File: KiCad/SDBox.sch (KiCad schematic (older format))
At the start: 18 parts, among them J1 DB25_Male, J2 Micro_SD_Card_Socket, U1 Rapberry_Pi_Pico_2W, U2 SN74CBT16210

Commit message: Add UART0_TX and UART0_RX through level shifter
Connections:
- net GND: no longer U2.7 (1A6), U2.9 (1A7)
- net RESET: now also U2.9 (1A7); no longer U2.6 (1A5)
- net RESET_3V3: now also U2.39 (1B7); no longer U2.42 (1B5)
- net UART0_TX_3V3: now reaches U1.16 (GP12)
- net UART0_TX_3V3: now also U2.42 (1B5)
- net UART0_RX_3V3: now reaches U1.17 (GP13)
- net UART0_RX_3V3: now also U2.40 (1B6)
- new net UART0_RX: U2.7 (1A6)
- new net UART0_TX: U2.6 (1A5)
- no-connect marks 12 -> 16
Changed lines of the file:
@@
 Text GLabel 7450 3600 1    50   Input ~ 0
 MOSI
-Text GLabel 2750 3450 0    50   BiDi ~ 0
-SELECT
 Text GLabel 7250 3600 1    50   Input ~ 0
 SCK
@@
 	1    0    0    -1
 $EndComp
-Text GLabel 3750 3550 2    50   BiDi ~ 0
-SELECT_3V3
 Text GLabel 3750 3350 2    50   BiDi ~ 0
 BUSY_3V3
@@
 Text GLabel 3750 3250 2    50   Input ~ 0
 ACK_3V3
-Text GLabel 2750 3550 0    50   Input ~ 0
+Text GLabel 2750 3850 0    50   Input ~ 0
 RESET
-Text GLabel 3750 3650 2    50   Output ~ 0
+Text GLabel 3750 3950 2    50   Output ~ 0
 RESET_3V3
 $Comp
@@
 $EndComp
 Wire Wire Line
-	2750 3650 2750 3750
-Wire Wire Line
-	2750 3750 2750 3850
-Connection ~ 2750 3750
-Connection ~ 2750 3850
-Wire Wire Line
-	2750 3850 2750 3950
-Connection ~ 2750 3950
-Wire Wire Line
 	2750 3950 2750 4050
 Connection ~ 2750 4050
@@
 NoConn ~ 3750 4150
 NoConn ~ 3750 4050
-NoConn ~ 3750 3950
-NoConn ~ 3750 3850
 $Comp
 L Device:D_Small D3
@@
 Text Label 2400 4450 0    50   ~ 0
 4V3
+NoConn ~ 4800 5200
+NoConn ~ 5800 4600
+NoConn ~ 5800 4400
+NoConn ~ 5800 4200
+NoConn ~ 5800 4100
+NoConn ~ 5800 3800
+Text GLabel 4800 4800 0    50   Output ~ 0
+UART0_TX_3V3
+Text GLabel 4800 4900 0    50   Input ~ 0
+UART0_RX_3V3
+Text GLabel 2750 3950 0    50   Input ~ 0
+GND
+Text GLabel 3750 3650 2    50   Input ~ 0
+UART0_TX_3V3
+Text GLabel 2750 3550 0    50   Output ~ 0
+UART0_TX
+Text GLabel 3750 3550 2    50   BiDi ~ 0
+SELECT_3V3
+Text GLabel 3750 3850 2    50   Output ~ 0
+UART0_RX_3V3
+Text GLabel 2750 3650 0    50   Input ~ 0
+UART0_RX
+Text GLabel 2750 3450 0    50   BiDi ~ 0
+SELECT
 $EndSCHEMATC

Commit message: Add UART pinheader on underside with TX0 (GP12), RX0 (GP13) and Power and GND
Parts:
- added J3: Conn_01x05, SDBox:UART_PinHeader_SMD_pads_2.54mm_pitch, symbol Connector_Generic:Conn_01x05
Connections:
- net +3V3: now also J3.1 (Pin_1)
- net +5V: now also J3.5 (Pin_5)
- net GND: now also J3.3 (Pin_3)
- net UART0_RX: now also J3.4 (Pin_4)
- net UART0_TX: now also J3.2 (Pin_2)
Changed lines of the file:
@@
 Text GLabel 2750 3450 0    50   BiDi ~ 0
 SELECT
+$Comp
+L Connector_Generic:Conn_01x05 J3
+U 1 1 6857FA47
+P 2900 6000
+F 0 "J3" V 2864 5712 50  0000 R CNN
+F 1 "Conn_01x05" V 2773 5712 50  0000 R CNN
+F 2 "SDBox:UART_PinHeader_SMD_pads_2.54mm_pitch" H 2900 6000 50  0001 C CNN
+F 3 "~" H 2900 6000 50  0001 C CNN
+	1    2900 6000
+	0    -1   -1   0
+$EndComp
+Text GLabel 2800 6200 3    50   Output ~ 0
+UART0_TX
+Text GLabel 3100 6200 3    50   Input ~ 0
+VCC
+Text GLabel 2900 6200 3    50   Input ~ 0
+GND
+Text GLabel 2700 6200 3    50   Input ~ 0
+3V3
+Text GLabel 3000 6200 3    50   Input ~ 0
+UART0_RX
 $EndSCHEMATC

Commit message: Improve routing
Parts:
- renumbered D2 to D1, D1 to D2
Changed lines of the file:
@@
 NoConn ~ 1550 3100
 $Comp
-L Device:LED D2
+L Device:LED D1
 U 1 1 5EBAFFCE
 P 8850 3150
-F 0 "D2" V 8889 3033 50  0000 R CNN
+F 0 "D1" V 8889 3033 50  0000 R CNN
 F 1 "Power LED indicator" V 8798 3033 50  0000 R CNN
 F 2 "LED_THT:LED_Rectangular_W5.0mm_H2.0mm" H 8850 3150 50  0001 C CNN
@@
 GND
 $Comp
-L Device:LED D1
+L Device:LED D2
 U 1 1 5EBA7223
 P 9100 4850
-F 0 "D1" V 9100 5000 50  0000 R CNN
+F 0 "D2" V 9100 5000 50  0000 R CNN
 F 1 "Activity LED indicator" V 9350 5150 50  0000 R CNN
 F 2 "LED_THT:LED_Rectangular_W5.0mm_H2.0mm" H 9100 4850 50  0001 C CNN

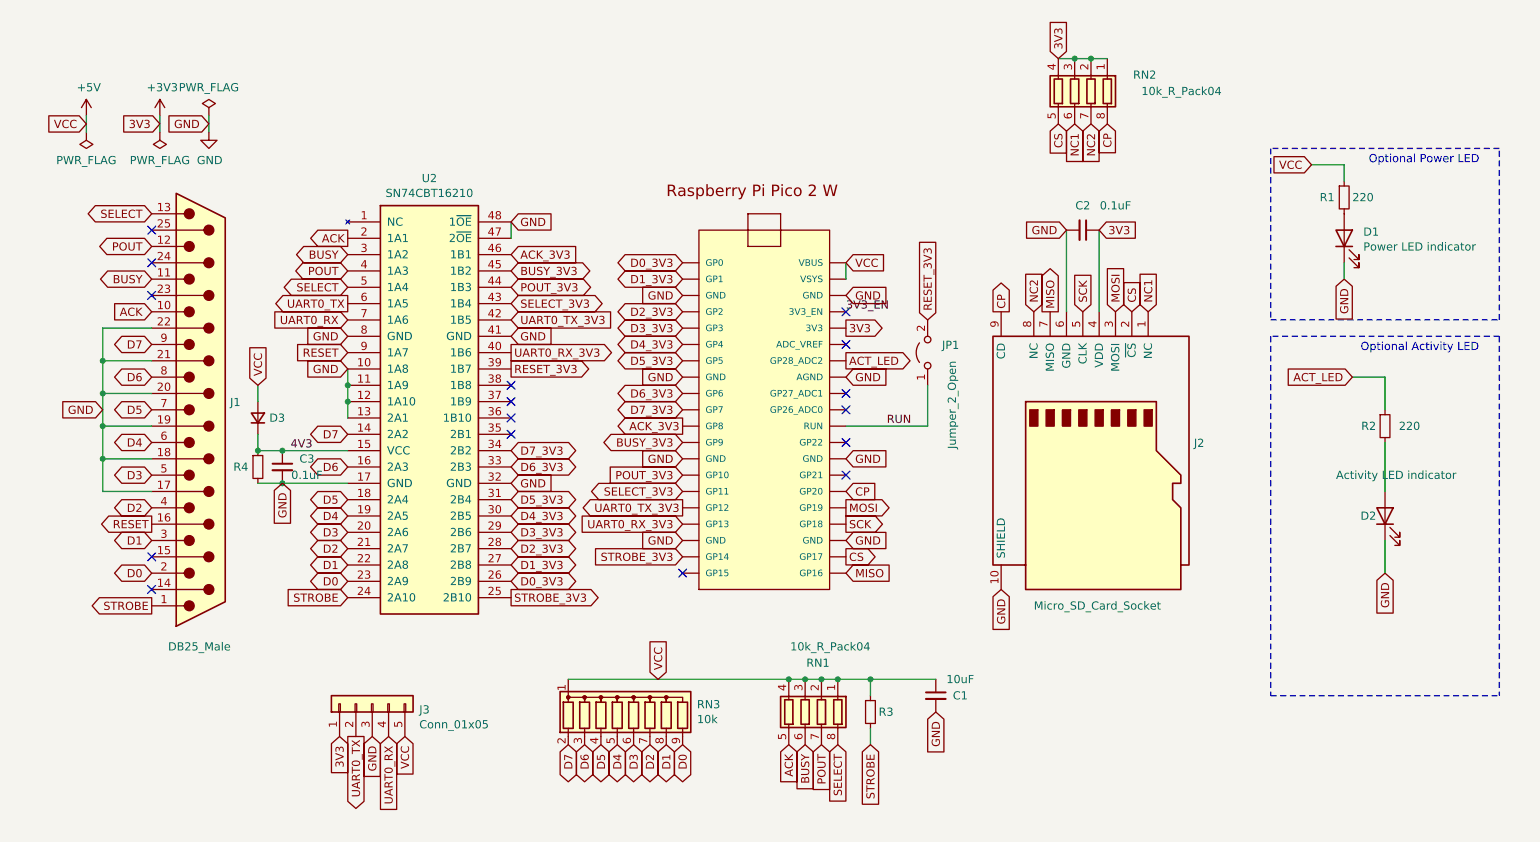
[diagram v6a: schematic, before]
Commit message: Change R1,R2 value from 220 to 330 Ohm, change D3 value from D_small to MMDL6050T1G
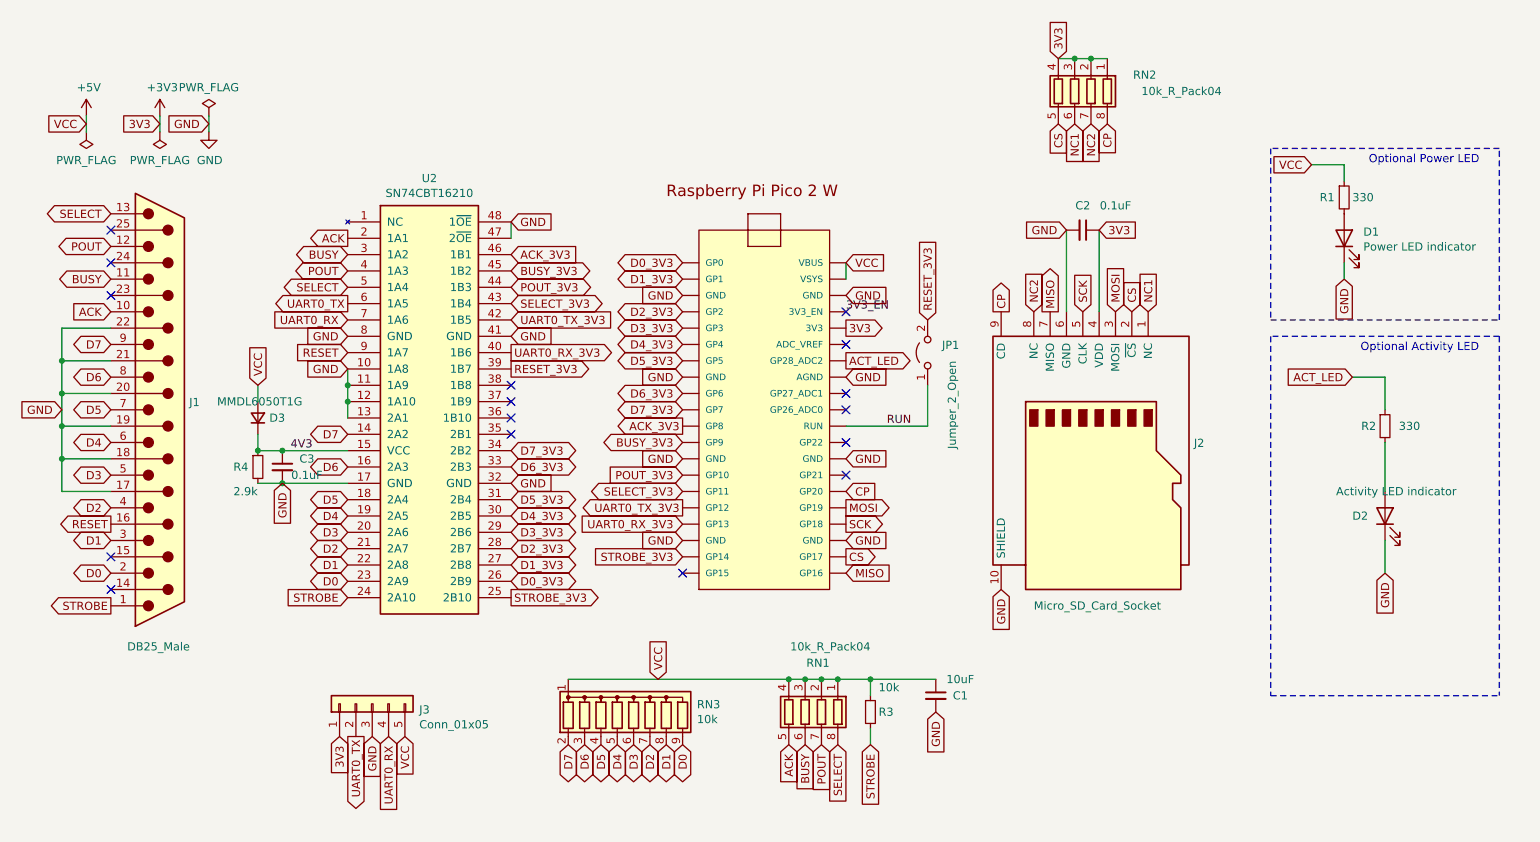
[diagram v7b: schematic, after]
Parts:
- D3: value D_Small -> MMDL6050T1G
- R1, R2: value 220 -> 330
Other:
- moved on the sheet: J1
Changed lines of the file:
@@
 Comment4 ""
 $EndDescr
-Text GLabel 1550 5200 0    50   BiDi ~ 0
+Text GLabel 1300 5200 0    50   BiDi ~ 0
 D0
-Text GLabel 1550 5000 0    50   BiDi ~ 0
+Text GLabel 1300 5000 0    50   BiDi ~ 0
 D1
-Text GLabel 1550 4800 0    50   BiDi ~ 0
+Text GLabel 1300 4800 0    50   BiDi ~ 0
 D2
-Text GLabel 1550 4600 0    50   BiDi ~ 0
+Text GLabel 1300 4600 0    50   BiDi ~ 0
 D3
-Text GLabel 1550 4400 0    50   BiDi ~ 0
+Text GLabel 1300 4400 0    50   BiDi ~ 0
 D4
-Text GLabel 1550 4200 0    50   BiDi ~ 0
+Text GLabel 1300 4200 0    50   BiDi ~ 0
 D5
-Text GLabel 1550 4000 0    50   BiDi ~ 0
+Text GLabel 1300 4000 0    50   BiDi ~ 0
 D6
-Text GLabel 1550 3800 0    50   BiDi ~ 0
+Text GLabel 1300 3800 0    50   BiDi ~ 0
 D7
-Text GLabel 1550 3400 0    50   BiDi ~ 0
+Text GLabel 1300 3400 0    50   BiDi ~ 0
 BUSY
-Text GLabel 1550 3200 0    50   BiDi ~ 0
+Text GLabel 1300 3200 0    50   BiDi ~ 0
 POUT
-Text GLabel 1550 3000 0    50   BiDi ~ 0
+Text GLabel 1300 3000 0    50   BiDi ~ 0
 SELECT
-Text GLabel 1250 4200 0    50   Input ~ 0
-GND
-Text GLabel 1550 4900 0    50   Output ~ 0
+Text GLabel 1000 4200 0    50   Input ~ 0
+GND
+Text GLabel 1300 4900 0    50   Output ~ 0
 RESET
 Text GLabel 5800 5000 2    50   Input ~ 0
@@
 Text GLabel 7250 3600 1    50   Input ~ 0
 SCK
-NoConn ~ 1550 3300
-NoConn ~ 1550 3500
-NoConn ~ 1550 5100
+NoConn ~ 1300 3300
+NoConn ~ 1300 3500
+NoConn ~ 1300 5100
 Text GLabel 5800 4900 2    50   Output ~ 0
 SCK
@@
 Text GLabel 1600 2450 0    50   Input ~ 0
 3V3
-NoConn ~ 1550 3100
+NoConn ~ 1300 3100
 $Comp
 L Device:LED D1
@@
 Wire Wire Line
 	8650 2700 8850 2700
-Text GLabel 1550 3600 0    50   Input ~ 0
+Text GLabel 1300 3600 0    50   Input ~ 0
 ACK
 $Comp
@@
 P 8850 2900
 F 0 "R1" H 8700 2900 50  0000 L CNN
-F 1 "220" H 8900 2900 50  0000 L CNN
+F 1 "330" H 8900 2900 50  0000 L CNN
 F 2 "Resistor_SMD:R_0805_2012Metric_Pad1.15x1.40mm_HandSolder" H 8850 2900 50  0001 C CNN
 F 3 "~" H 8850 2900 50  0001 C CNN
@@
 Optional Power LED
 Wire Wire Line
-	1550 3700 1250 3700
-Wire Wire Line
-	1250 3700 1250 3900
-Wire Wire Line
-	1250 4700 1550 4700
-Wire Wire Line
-	1550 3900 1250 3900
-Connection ~ 1250 3900
-Wire Wire Line
-	1250 3900 1250 4100
-Wire Wire Line
-	1550 4100 1250 4100
-Connection ~ 1250 4100
-Wire Wire Line
-	1250 4100 1250 4300
-Wire Wire Line
-	1550 4300 1250 4300
-Connection ~ 1250 4300
-Wire Wire Line
-	1250 4300 1250 4500
-Wire Wire Line
-	1550 4500 1250 4500
-Connection ~ 1250 4500
-Wire Wire Line
-	1250 4500 1250 4700
+	1300 3700 1000 3700
+Wire Wire Line
+	1000 3700 1000 3900
+Wire Wire Line
+	1000 4700 1300 4700
+Wire Wire Line
+	1300 3900 1000 3900
+Connection ~ 1000 3900
+Wire Wire Line
+	1000 3900 1000 4100
+Wire Wire Line
+	1300 4100 1000 4100
+Connection ~ 1000 4100
+Wire Wire Line
+	1000 4100 1000 4300
+Wire Wire Line
+	1300 4300 1000 4300
+Connection ~ 1000 4300
+Wire Wire Line
+	1000 4300 1000 4500
+Wire Wire Line
+	1300 4500 1000 4500
+Connection ~ 1000 4500
+Wire Wire Line
+	1000 4500 1000 4700
 Text GLabel 2750 3150 0    50   Output ~ 0
 ACK
@@
 L Connector:DB25_Male J1
 U 1 1 6108B66B
-P 1850 4200
-F 0 "J1" H 2030 4246 50  0000 L CNN
-F 1 "DB25_Male" H 1650 2750 50  0000 L CNN
-F 2 "Connector_Dsub:DSUB-25_Male_EdgeMount_P2.77mm" H 1850 4200 50  0001 C CNN
-F 3 " ~" H 1850 4200 50  0001 C CNN
-	1    1850 4200
+P 1600 4200
+F 0 "J1" H 1780 4246 50  0000 L CNN
+F 1 "DB25_Male" H 1400 2750 50  0000 L CNN
+F 2 "Connector_Dsub:DSUB-25_Male_EdgeMount_P2.77mm" H 1600 4200 50  0001 C CNN
+F 3 " ~" H 1600 4200 50  0001 C CNN
+	1    1600 4200
 	1    0    0    -1
 $EndComp
@@
 D7_3V3
 NoConn ~ 3750 4350
-Text GLabel 1550 5400 0    50   Output ~ 0
+Text GLabel 1300 5400 0    50   Output ~ 0
 STROBE
 Text GLabel 2750 5350 0    50   Input ~ 0
@@
 U 1 1 5EBA7223
 P 9100 4850
-F 0 "D2" V 9100 5000 50  0000 R CNN
-F 1 "Activity LED indicator" V 9350 5150 50  0000 R CNN
+F 0 "D2" V 9100 5050 50  0000 R CNN
+F 1 "Activity LED indicator" V 9250 5150 50  0000 R CNN
 F 2 "LED_THT:LED_Rectangular_W5.0mm_H2.0mm" H 9100 4850 50  0001 C CNN
 F 3 "~" H 9100 4850 50  0001 C CNN
@@
 P 9100 4300
 F 0 "R2" H 9000 4300 50  0000 C CNN
-F 1 "220" H 9250 4300 50  0000 C CNN
+F 1 "330" H 9250 4300 50  0000 C CNN
 F 2 "Resistor_SMD:R_0805_2012Metric_Pad1.15x1.40mm_HandSolder" H 9100 4300 50  0001 C CNN
 F 3 "~" H 9100 4300 50  0001 C CNN
@@
 P 5950 6050
 F 0 "R3" H 6000 6050 50  0000 L CNN
-F 1 "10k" H 5750 6050 50  0001 L CNN
+F 1 "10k" H 6000 6200 50  0000 L CNN
 F 2 "Resistor_SMD:R_0603_1608Metric_Pad0.98x0.95mm_HandSolder" H 5950 6050 50  0001 C CNN
 F 3 "~" H 5950 6050 50  0001 C CNN
@@
 Text GLabel 7400 2450 3    50   Input ~ 0
 CP
-NoConn ~ 1550 5300
+NoConn ~ 1300 5300
 Text GLabel 4650 5850 1    50   Input ~ 0
 VCC
@@
 P 2200 4250
 F 0 "D3" V 2200 4180 50  0000 R CNN
-F 1 "D_Small" V 2155 4180 50  0001 R CNN
+F 1 "MMDL6050T1G" V 2300 4500 50  0000 R CNN
 F 2 "Diode_SMD:D_0603_1608Metric_Pad1.05x0.95mm_HandSolder" V 2200 4250 50  0001 C CNN
 F 3 "~" V 2200 4250 50  0001 C CNN
@@
 P 2200 4550
 F 0 "R4" H 2050 4550 50  0000 L CNN
-F 1 "2.9k" H 2000 4550 50  0001 L CNN
+F 1 "2.9k" H 2050 4400 50  0000 L CNN
 F 2 "Resistor_SMD:R_0603_1608Metric_Pad0.98x0.95mm_HandSolder" H 2200 4550 50  0001 C CNN
 F 3 "~" H 2200 4550 50  0001 C CNN

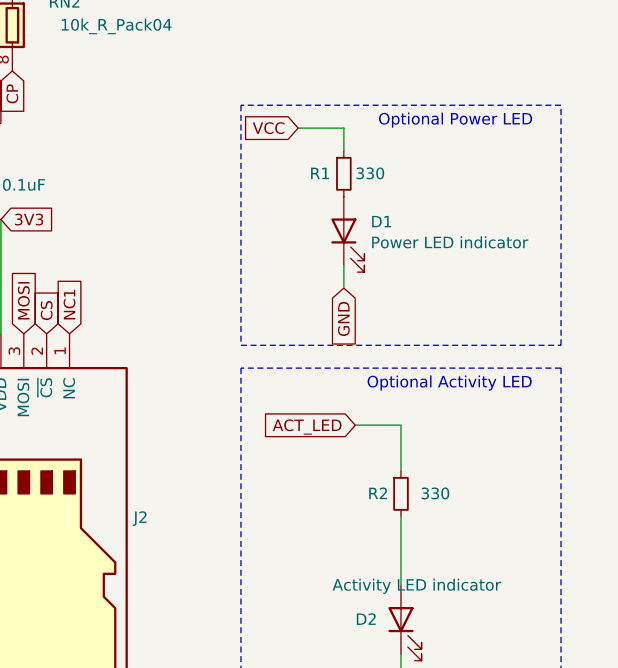
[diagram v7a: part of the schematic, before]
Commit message: Change R1 value from 330 to 4.7k, Change R2 value from 330 to 220
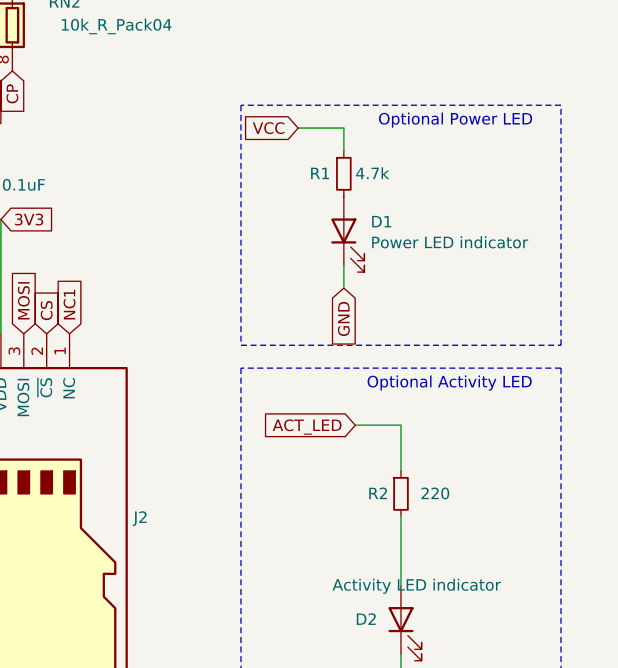
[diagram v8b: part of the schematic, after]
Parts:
- R1: value 330 -> 4.7k
- R2: value 330 -> 220
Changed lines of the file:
@@
 P 8850 2900
 F 0 "R1" H 8700 2900 50  0000 L CNN
-F 1 "330" H 8900 2900 50  0000 L CNN
+F 1 "4.7k" H 8900 2900 50  0000 L CNN
 F 2 "Resistor_SMD:R_0805_2012Metric_Pad1.15x1.40mm_HandSolder" H 8850 2900 50  0001 C CNN
 F 3 "~" H 8850 2900 50  0001 C CNN
@@
 P 9100 4300
 F 0 "R2" H 9000 4300 50  0000 C CNN
-F 1 "330" H 9250 4300 50  0000 C CNN
+F 1 "220" H 9250 4300 50  0000 C CNN
 F 2 "Resistor_SMD:R_0805_2012Metric_Pad1.15x1.40mm_HandSolder" H 9100 4300 50  0001 C CNN
 F 3 "~" H 9100 4300 50  0001 C CNN
